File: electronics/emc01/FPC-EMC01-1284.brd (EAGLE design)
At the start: 160 x 100 mm, 89 parts, among them J4 PCIE, J8 CON-HDMI, J9 CON-FFC-SFW15R, SW1 SPST_TACT-EVQQ2, U1 LM2841, U10 MCP4728, U2 A4982, U3 A4982, U4 A4982, U5 ATMEGA1284P-AU, U7 AP7313

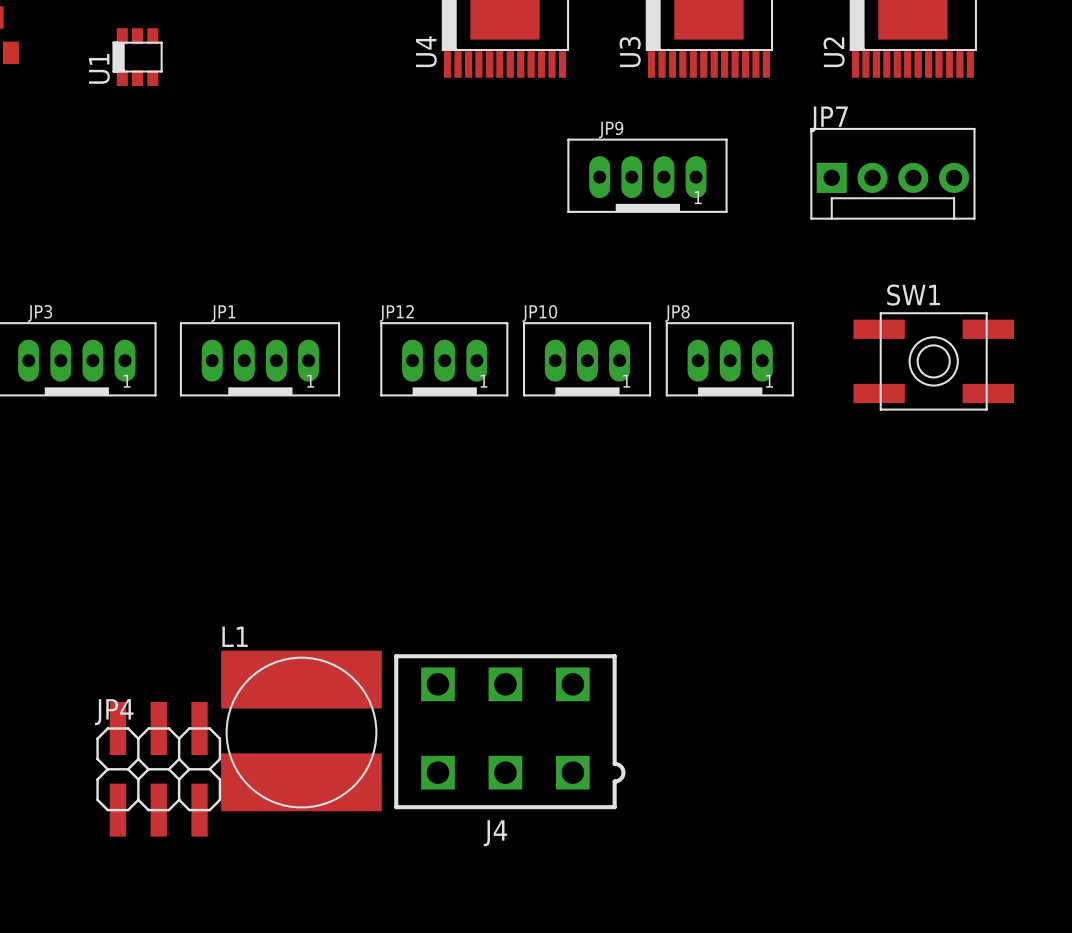
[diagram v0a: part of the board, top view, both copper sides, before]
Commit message: Fixed schematics
looks more uniform
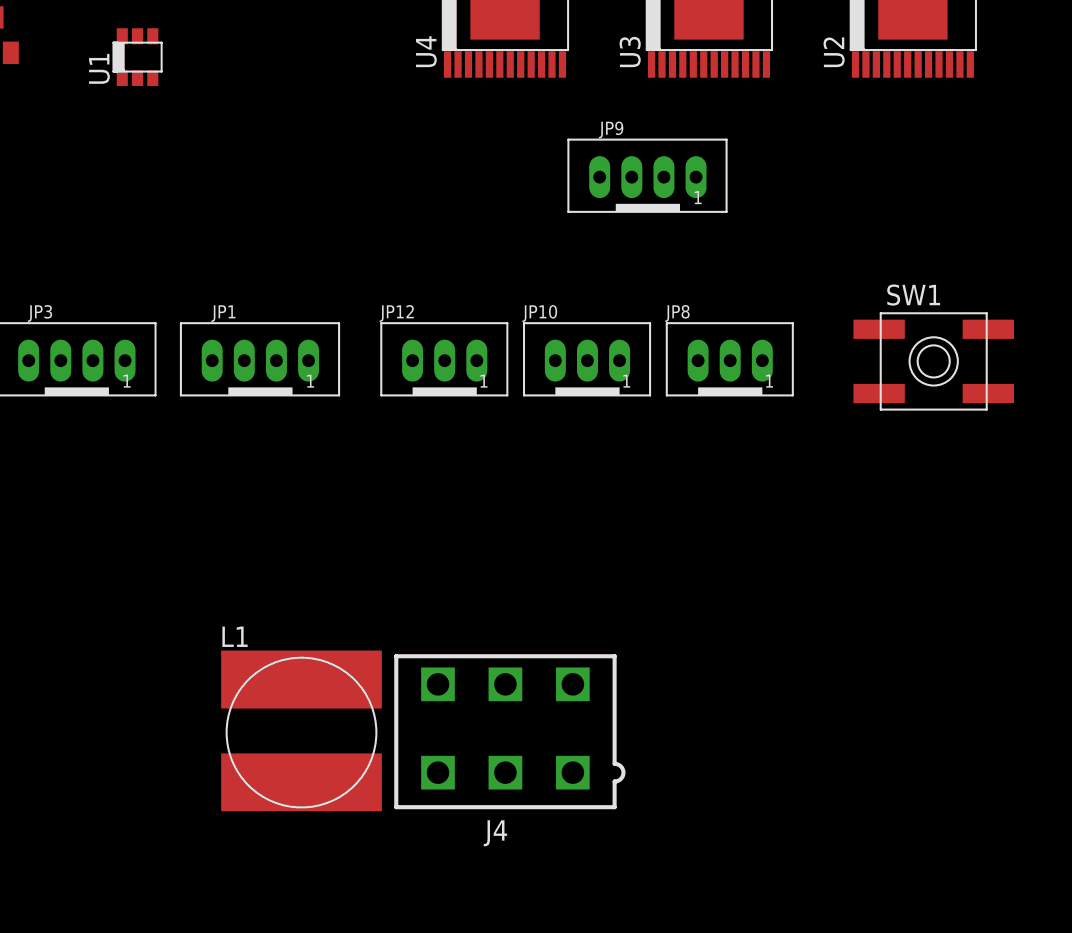
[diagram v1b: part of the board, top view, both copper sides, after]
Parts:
- removed JP4: ICSP, pinhead-2:2X03SMD
- removed JP7: I2C, SparkFun:MOLEX-1X4
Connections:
- net !RESET: no longer JP4.2
- net +5V: no longer JP4.5, JP7.4
- net GND: no longer JP4.1, JP7.3
- net MISO: no longer JP4.6
- net MOSI: no longer JP4.3
- net SCL: no longer JP7.1
- net SCLK: no longer JP4.4
- net SDA: no longer JP7.2
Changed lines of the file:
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@@
 <?xml version="1.0" encoding="utf-8"?>
 <!DOCTYPE eagle SYSTEM "eagle.dtd">
-<eagle version="6.5.0">
+<eagle version="6.6.0">
 <drawing>
 <settings>
@@
 <element name="JP8" library="SRG" package="JST_B3B-PH_HEADER" value="Y-STOP" x="-40.64" y="30.48"/>
 <element name="JP10" library="SRG" package="JST_B3B-PH_HEADER" value="Z-STOP" x="-49.53" y="30.48"/>
-<element name="JP4" library="pinhead-2" package="2X03SMD" value="ICSP" x="-77.47" y="6.35"/>
 <element name="C7" library="rcl" package="PANASONIC_D" value="100uF" x="-67.31" y="60.96"/>
 <element name="C38" library="ipc-7351-capacitor" package="CAPC2012X145AN" value="0.1uF" x="-87.63" y="74.93"/>
@@
 <attribute name="OC_FARNELL" value="unknown" x="0" y="0" size="1.778" layer="27" display="off"/>
 </element>
-<element name="JP7" library="SparkFun" package="MOLEX-1X4" value="I2C" x="-34.29" y="41.91"/>
 <element name="SW1" library="adafruit" package="EVQ-Q2" value="SPST_TACT-EVQQ2" x="-27.94" y="30.48"/>
 <element name="R5" library="adafruit" package="R0805" value="100K" x="-88.9" y="93.98"/>
@@
 <contactref element="JP10" pad="P3"/>
 <contactref element="C7" pad="-"/>
-<contactref element="JP4" pad="1"/>
 <contactref element="LED1" pad="C"/>
 <contactref element="R17" pad="2"/>
@@
 <contactref element="U7" pad="3"/>
 <contactref element="C32" pad="2"/>
-<contactref element="JP7" pad="3"/>
 <contactref element="SW1" pad="A"/>
 <contactref element="SW1" pad="A'"/>
@@
 <wire x1="-101.92" y1="-7.62" x2="-103.82" y2="-11.43" width="0" layer="19" extent="1-1"/>
 <wire x1="-101.92" y1="-3.81" x2="-101.92" y2="-7.62" width="0" layer="19" extent="1-1"/>
-<wire x1="-78.74" y1="2.54" x2="-101.92" y2="-3.81" width="0" layer="19" extent="1-1"/>
-<wire x1="-58.81" y1="10.37" x2="-78.74" y2="2.54" width="0" layer="19" extent="1-1"/>
+<wire x1="-58.81" y1="10.37" x2="-101.92" y2="-3.81" width="0" layer="19" extent="1-1"/>
 <wire x1="-54.61" y1="10.37" x2="-58.81" y2="10.37" width="0" layer="19" extent="1-1"/>
 <wire x1="-50.41" y1="10.37" x2="-54.61" y2="10.37" width="0" layer="19" extent="1-1"/>
@@
 <wire x1="-31.34" y1="28.48" x2="-42.6125" y2="30.5275" width="0" layer="19" extent="1-1"/>
 <wire x1="-24.54" y1="28.48" x2="-31.34" y2="28.48" width="0" layer="19" extent="1-1"/>
-<wire x1="-29.21" y1="41.91" x2="-31.34" y2="28.48" width="0" layer="19" extent="1-1"/>
-<wire x1="-29.235" y1="52.02" x2="-29.21" y2="41.91" width="0" layer="19" extent="1-1"/>
+<wire x1="-41.935" y1="52.02" x2="-42.6125" y2="30.5275" width="0" layer="19" extent="1-1"/>
+<wire x1="-38.36" y1="55.07" x2="-41.935" y2="52.02" width="0" layer="19" extent="1-1"/>
+<wire x1="-45.51" y1="55.07" x2="-41.935" y2="52.02" width="0" layer="19" extent="1-1"/>
+<wire x1="-32.81" y1="55.07" x2="-38.36" y2="55.07" width="0" layer="19" extent="1-1"/>
+<wire x1="-29.235" y1="52.02" x2="-32.81" y2="55.07" width="0" layer="19" extent="1-1"/>
 <wire x1="-25.66" y1="55.07" x2="-29.235" y2="52.02" width="0" layer="19" extent="1-1"/>
-<wire x1="-32.81" y1="55.07" x2="-29.235" y2="52.02" width="0" layer="19" extent="1-1"/>
-<wire x1="-38.36" y1="55.07" x2="-32.81" y2="55.07" width="0" layer="19" extent="1-1"/>
-<wire x1="-41.935" y1="52.02" x2="-38.36" y2="55.07" width="0" layer="19" extent="1-1"/>
-<wire x1="-45.51" y1="55.07" x2="-41.935" y2="52.02" width="0" layer="19" extent="1-1"/>
 <wire x1="-51.06" y1="55.07" x2="-45.51" y2="55.07" width="0" layer="19" extent="1-1"/>
 <wire x1="-54.635" y1="52.02" x2="-51.06" y2="55.07" width="0" layer="19" extent="1-1"/>
@@
 </signal>
 <signal name="!RESET">
-<contactref element="JP4" pad="2"/>
 <contactref element="JP2" pad="2"/>
-<wire x1="-78.74" y1="7.62" x2="-140.97" y2="-276.86" width="0" layer="19" extent="1-1"/>
 </signal>
 <signal name="12V">
@@
 </signal>
 <signal name="MISO">
-<contactref element="JP4" pad="6"/>
 <contactref element="U5" pad="2"/>
 <contactref element="JP2" pad="6"/>
-<wire x1="-73.66" y1="7.62" x2="-135.89" y2="-276.86" width="0" layer="19" extent="1-1"/>
-<wire x1="72.417896875" y1="21.063946875" x2="-73.66" y2="7.62" width="0" layer="19" extent="1-1"/>
+<wire x1="72.417896875" y1="21.063946875" x2="-135.89" y2="-276.86" width="0" layer="19" extent="1-1"/>
 </signal>
 <signal name="MOSI">
-<contactref element="JP4" pad="3"/>
 <contactref element="U5" pad="1"/>
 <contactref element="JP2" pad="3"/>
-<wire x1="-76.2" y1="2.54" x2="-138.43" y2="-281.94" width="0" layer="19" extent="1-1"/>
-<wire x1="71.861121875" y1="21.620721875" x2="-76.2" y2="2.54" width="0" layer="19" extent="1-1"/>
+<wire x1="71.861121875" y1="21.620721875" x2="-138.43" y2="-281.94" width="0" layer="19" extent="1-1"/>
 </signal>
 <signal name="X-STOP">
@@
 </signal>
 <signal name="SCLK">
-<contactref element="JP4" pad="4"/>
 <contactref element="U5" pad="3"/>
 <contactref element="JP2" pad="4"/>
-<wire x1="-76.2" y1="7.62" x2="-138.43" y2="-276.86" width="0" layer="19" extent="1-1"/>
-<wire x1="72.992634375" y1="20.489209375" x2="-76.2" y2="7.62" width="0" layer="19" extent="1-1"/>
+<wire x1="72.992634375" y1="20.489209375" x2="-138.43" y2="-276.86" width="0" layer="19" extent="1-1"/>
 </signal>
 <signal name="!XYZ-ENABLE">
@@
 <contactref element="C1" pad="1"/>
 <contactref element="L1" pad="P$2"/>
-<contactref element="JP4" pad="5"/>
 <contactref element="JP12" pad="P2"/>
 <contactref element="JP8" pad="P2"/>
@@
 <contactref element="R27" pad="1"/>
 <contactref element="U7" pad="1"/>
-<contactref element="JP7" pad="4"/>
 <contactref element="R5" pad="2"/>
 <contactref element="C13" pad="2"/>
@@
 <wire x1="-101.92" y1="-15.24" x2="-101.92" y2="-19.05" width="0" layer="19" extent="1-1"/>
 <wire x1="-101.92" y1="-11.43" x2="-101.92" y2="-15.24" width="0" layer="19" extent="1-1"/>
-<wire x1="-73.66" y1="2.54" x2="-101.92" y2="-11.43" width="0" layer="19" extent="1-1"/>
-<wire x1="-67.31" y1="4.2672" x2="-73.66" y2="2.54" width="0" layer="19" extent="1-1"/>
+<wire x1="-67.31" y1="4.2672" x2="-101.92" y2="-11.43" width="0" layer="19" extent="1-1"/>
 <wire x1="-58.3925" y1="30.5275" x2="-67.31" y2="4.2672" width="0" layer="19" extent="1-1"/>
 <wire x1="-49.5025" y1="30.5275" x2="-58.3925" y2="30.5275" width="0" layer="19" extent="1-1"/>
 <wire x1="-40.6125" y1="30.5275" x2="-49.5025" y2="30.5275" width="0" layer="19" extent="1-1"/>
-<wire x1="-26.67" y1="41.91" x2="-40.6125" y2="30.5275" width="0" layer="19" extent="1-1"/>
-<wire x1="-26.96" y1="48.97" x2="-26.67" y2="41.91" width="0" layer="19" extent="1-1"/>
-<wire x1="-29.56" y1="48.97" x2="-26.96" y2="48.97" width="0" layer="19" extent="1-1"/>
-<wire x1="-30.21" y1="48.97" x2="-29.56" y2="48.97" width="0" layer="19" extent="1-1"/>
-<wire x1="-39.66" y1="48.97" x2="-30.21" y2="48.97" width="0" layer="19" extent="1-1"/>
+<wire x1="-39.66" y1="48.97" x2="-40.6125" y2="30.5275" width="0" layer="19" extent="1-1"/>
 <wire x1="-42.26" y1="48.97" x2="-39.66" y2="48.97" width="0" layer="19" extent="1-1"/>
 <wire x1="-42.91" y1="48.97" x2="-42.26" y2="48.97" width="0" layer="19" extent="1-1"/>
+<wire x1="-30.21" y1="48.97" x2="-39.66" y2="48.97" width="0" layer="19" extent="1-1"/>
+<wire x1="-29.56" y1="48.97" x2="-30.21" y2="48.97" width="0" layer="19" extent="1-1"/>
+<wire x1="-26.96" y1="48.97" x2="-29.56" y2="48.97" width="0" layer="19" extent="1-1"/>
 <wire x1="-52.36" y1="48.97" x2="-42.91" y2="48.97" width="0" layer="19" extent="1-1"/>
 <wire x1="-54.96" y1="48.97" x2="-52.36" y2="48.97" width="0" layer="19" extent="1-1"/>
@@
 <wire x1="-31.38" y1="81.28" x2="-30.21" y2="87.63" width="0" layer="19" extent="1-1"/>
 <wire x1="-45.99" y1="93.98" x2="-42.91" y2="87.63" width="0" layer="19" extent="1-1"/>
-<wire x1="75.2377" y1="27.47585" x2="-26.67" y2="41.91" width="0" layer="19" extent="1-1"/>
+<wire x1="75.2377" y1="27.47585" x2="-26.96" y2="48.97" width="0" layer="19" extent="1-1"/>
 <wire x1="83.35585" y1="26.362296875" x2="75.2377" y2="27.47585" width="0" layer="19" extent="1-1"/>
 <wire x1="82.799075" y1="18.800921875" x2="83.35585" y2="26.362296875" width="0" layer="19" extent="1-1"/>
@@
 </signal>
 <signal name="SCL" class="1">
-<contactref element="JP7" pad="1"/>
 <contactref element="U10" pad="2"/>
 <contactref element="J1" pad="6"/>
@@
 <contactref element="J6" pad="6"/>
 <contactref element="JP5" pad="1"/>
-<wire x1="-34.29" y1="41.91" x2="-122.42" y2="-53" width="0" layer="19" extent="1-1"/>
 <wire x1="-135.89" y1="-187.96" x2="-122.42" y2="-53" width="0" layer="19" extent="1-1"/>
 <wire x1="-135.89" y1="-195.58" x2="-135.89" y2="-187.96" width="0" layer="19" extent="1-1"/>
@@
 </signal>
 <signal name="SDA" class="1">
-<contactref element="JP7" pad="2"/>
 <contactref element="U10" pad="3"/>
 <contactref element="J1" pad="5"/>
@@
 <contactref element="J6" pad="5"/>
 <contactref element="JP5" pad="2"/>
-<wire x1="-31.75" y1="41.91" x2="-121.92" y2="-53" width="0" layer="19" extent="1-1"/>
 <wire x1="-135.89" y1="-190.5" x2="-121.92" y2="-53" width="0" layer="19" extent="1-1"/>
 <wire x1="-135.89" y1="-198.12" x2="-135.89" y2="-190.5" width="0" layer="19" extent="1-1"/>

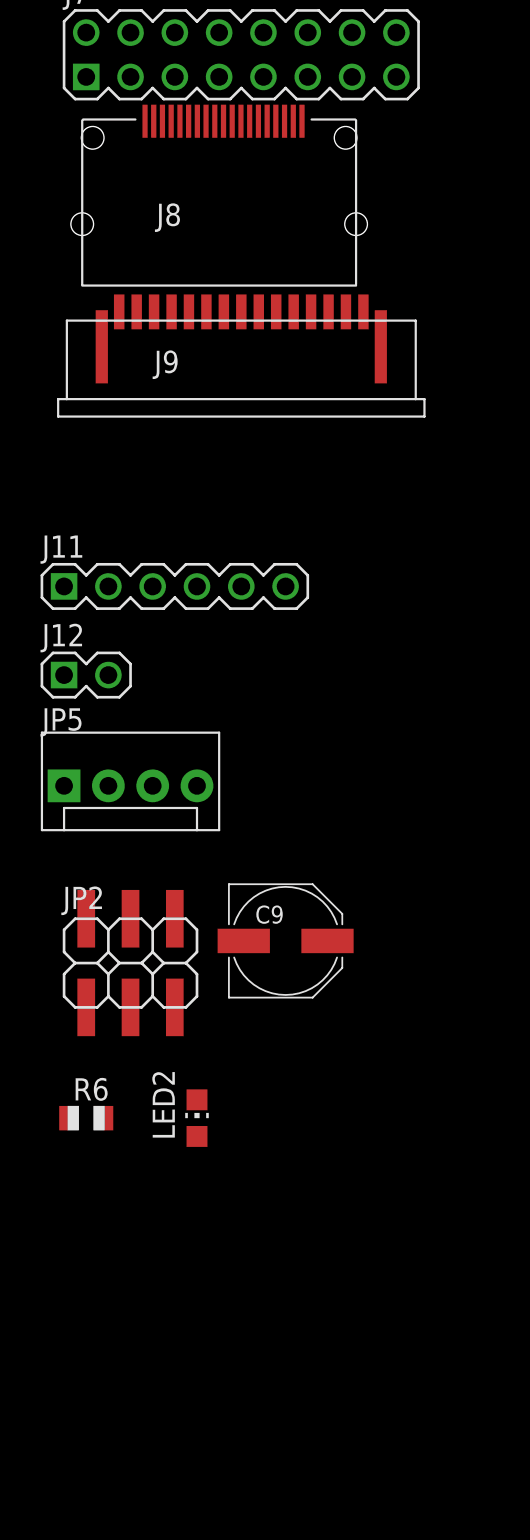
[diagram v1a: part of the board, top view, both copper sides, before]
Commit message: Added FFC connector from HDMI
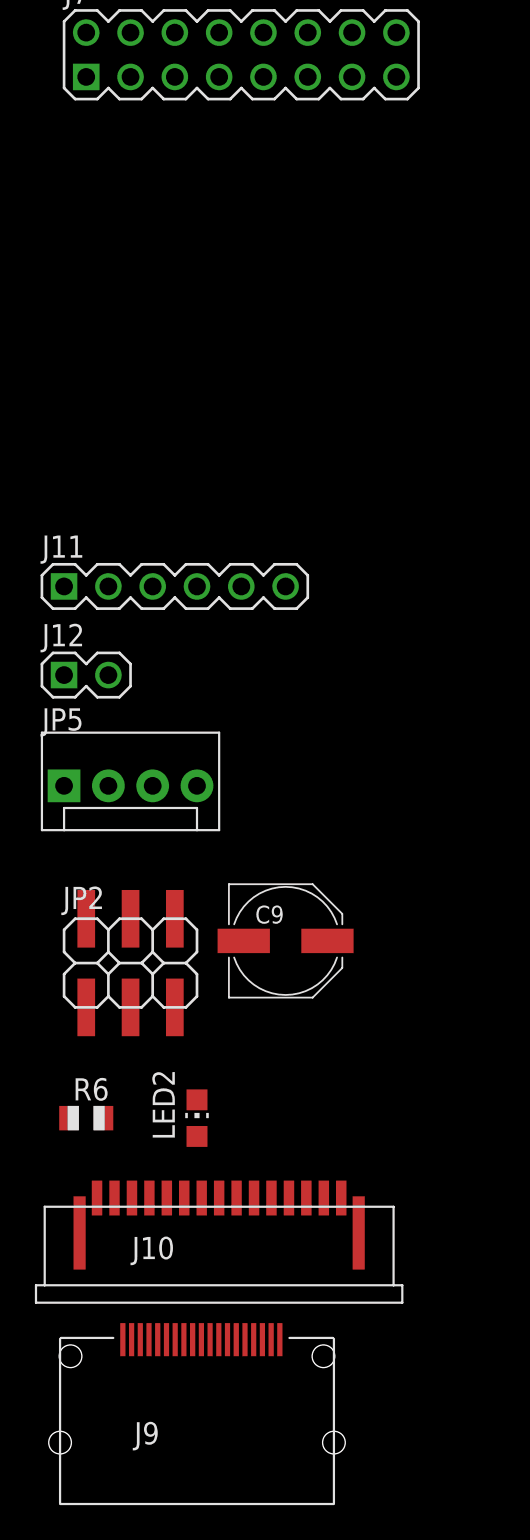
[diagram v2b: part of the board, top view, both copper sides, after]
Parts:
- removed J8: CON-HDMI, !NJ SMT:CON-HDMI-FCI-10029449-001RLF
- added J10: CON-FFC-SFW15R, !NJ SMT:CON-FFC-SFW15R
- J9: value CON-FFC-SFW15R -> CON-HDMI; device !NJ SMT:CON-FFC-SFW15R -> !NJ SMT:CON-HDMI-FCI-10029449-001RLF
- moved J9 58.5 mm to (-134.6, -301.0)
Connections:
- new net CAM1_CN: J10.8, J9.12
- new net CAM1_CP: J10.9, J9.10
- new net CAM1_DN0: J10.2, J9.9
- new net CAM1_DN1: J10.5, J9.6
- new net CAM1_DP0: J10.3, J9.7
- new net CAM1_DP1: J10.6, J9.4
- new net CAM_CLK: J10.12, J9.1
- new net CAM_GPIO: J10.11, J9.19
- new net SCL0: J10.13, J9.15
- new net SDA0: J10.14, J9.16
- net +5V: now also J10.15, J9.18
- net GND: now also J10.1, J10.10, J10.4, J10.7, J9.11, J9.13, J9.14, J9.17, J9.2, J9.3, J9.5, J9.8

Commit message: Fixed errors/connectors
Fixed the ERC errors, ones that are left just ignore. Neil needs to add
his library of proper JST connectors to the board and we will be pretty
much ready to route.
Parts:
- removed J11: (no value), !con-lstb:MA06-1
- removed J12: (no value), !con-lstb:MA02-1
- removed J2: (no value), !con-lstb:MA13-2
- removed JP12: X-STOP, SRG:JST_B3B-PH_HEADER
- added JP11: (no value), pinhead-2:1X03SMD/90
- added JP4: (no value), pinhead-2:2X13SMD
- added JP6: (no value), pinhead-2:1X06SMD
- added JP7: (no value), pinhead-2:1X02SMD
- C13, C14, C34, C36, C42: value (none) -> 100nF
- J1, J3, J5, J6, J7: device !con-lstb:MA08-2 -> pinhead-2:2X08SMD
- JP10: value Z-STOP -> (none); device SRG:JST_B3B-PH_HEADER -> pinhead-2:1X03SMD/90
- JP5: value I2C -> (none); device SparkFun:MOLEX-1X4 -> pinhead-2:1X04SMD
- JP8: value Y-STOP -> (none); device SRG:JST_B3B-PH_HEADER -> pinhead-2:1X03SMD/90
- Q4: value (none) -> 16Mhz
- moved JP10 377.5 mm to (-165.1, -328.9)
- moved JP8 376.4 mm to (-152.4, -328.9)
- moved JP5 80.1 mm to (-179.1, -340.4)
- moved U5 18.2 mm to (86.4, 39.4)
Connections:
- net X-DIR renamed X_DIR
- net X-STEP renamed X_STEP
- net Y-DIR renamed Y_DIR
- net Y-STEP renamed Y_STEP
- removed net !RESET: JP2.2
- removed net /XYZENABLE: U5.15
- removed net RESET: R5.1, SW1.B, SW1.B', U5.4
- removed net Z-DIR: U4.14
- removed net Z-STEP: U4.11
- new net !~RESET: JP2.2, R5.1, SW1.B, SW1.B', U5.4
- new net N$1: LED1.A, R1.1
- new net N$2: LED2.A, R6.1
- net !XYZ-ENABLE: now also U5.15
- net +3V3_RASPI: now also JP4.1, JP4.17; no longer J2.1, J2.17
- net +5V: now also JP10.2, JP11.2, JP4.2, JP4.4, JP5.1, JP6.4, JP8.2; no longer J11.4, J2.2, J2.4, JP10.P2, JP12.P2, JP5.4, JP8.P2
- net AVR_RXD: now also JP6.3; no longer J11.3
- net AVR_TXD: now also JP6.2; no longer J11.2
- net DTR: now also JP6.1; no longer J11.1
- net GND: now also JP10.3, JP11.3, JP4.14, JP4.20, JP4.25, JP4.6, JP4.9, JP5.2, JP6.5, JP6.6, JP8.3; no longer J11.5, J11.6, J2.14, J2.20, J2.25, J2.6, J2.9, JP10.P3, JP12.P3, JP5.3, JP8.P3
- net LCD_/E: now also JP4.18; no longer J2.18
- net LCD_DB4: now also JP4.16; no longer J2.16
- net LCD_DB5: now also JP4.11; no longer J2.11
- net LCD_DB6: now also JP4.13; no longer J2.13
- net LCD_DB7: now also JP4.15; no longer J2.15
- net LCD_RS: now also JP4.22; no longer J2.22
- net PANEL_ENC_A: now also JP4.26; no longer J2.26
- net PANEL_ENC_B: now also JP4.21; no longer J2.21
- net PANEL_ENC_SW: now also JP4.24; no longer J2.24
- net PANEL_LED_GRN: now also JP4.19; no longer J2.19
- net PANEL_LED_RED: now also JP4.12; no longer J2.12
- net PANEL_PUSHBTN: now also JP4.23; no longer J2.23
- net RASPI_RXD: now also JP4.10, JP7.1; no longer J12.1, J2.10
- net RASPI_TXD: now also JP4.8, JP7.2; no longer J12.2, J2.8
- net SCL: now also JP5.4, U5.19; no longer JP5.1
- net SDA: now also JP5.3, U5.20; no longer JP5.2
- net X-STOP: now also JP8.1; no longer JP12.P1
- net XTAL2: now also U5.7
- net Y-STOP: now also JP10.1; no longer JP8.P1
- net Z-STOP: now also JP11.1; no longer JP10.P1
- net Z_DIR: now also U4.14
- net Z_STEP: now also U4.11
